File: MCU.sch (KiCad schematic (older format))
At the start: 25 parts, among them J1 Conn_ARM_SWD_NXP, J4 Conn_ARM_JTAG_SWD_20, U1 LPC54616J512, Y1 12MHz, Y2 32.768k

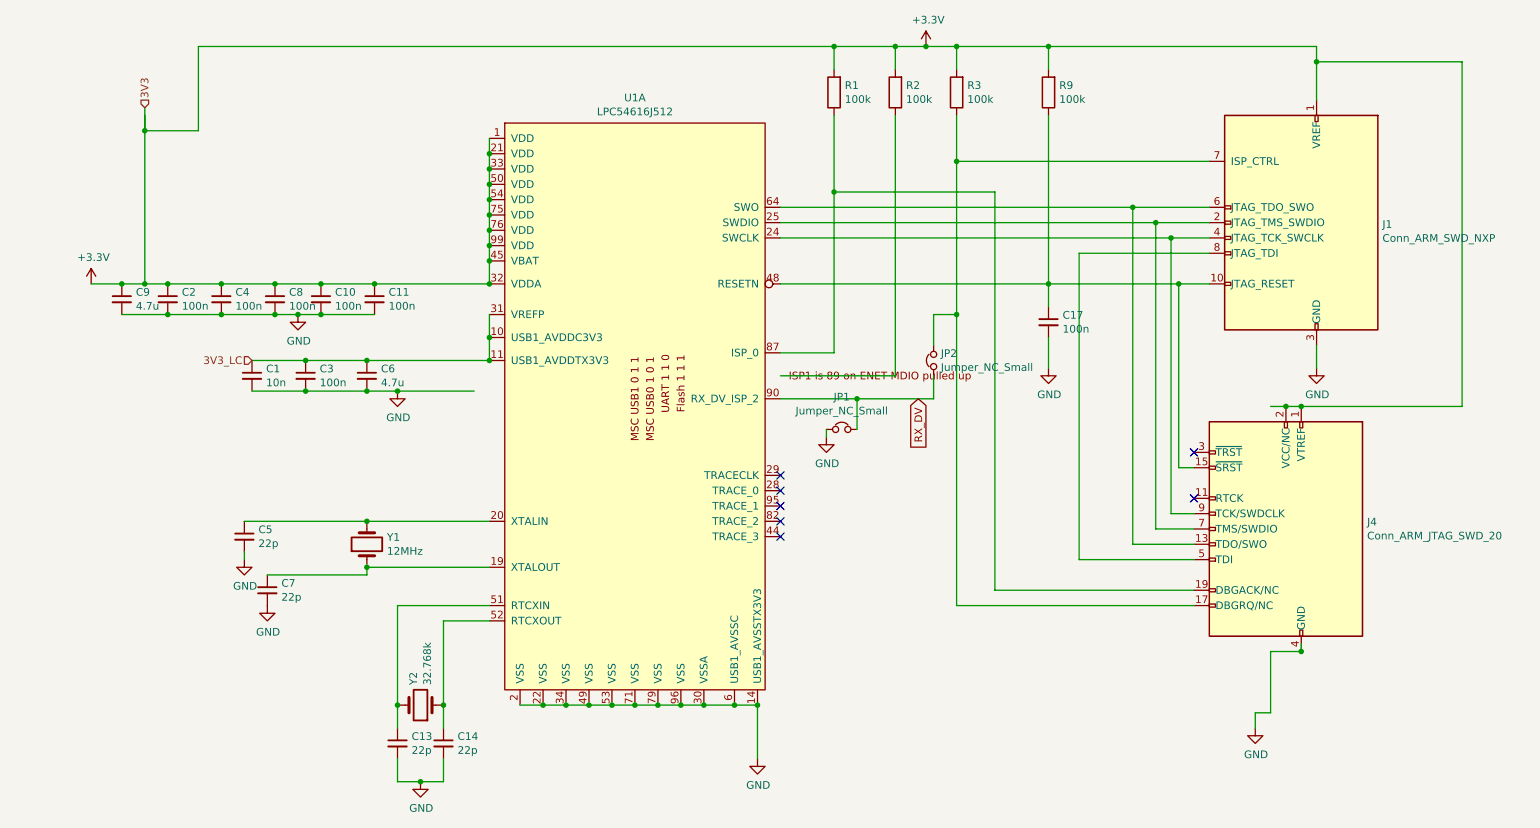
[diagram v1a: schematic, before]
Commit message: V3 bigger board, RMII instrumentation, inverter
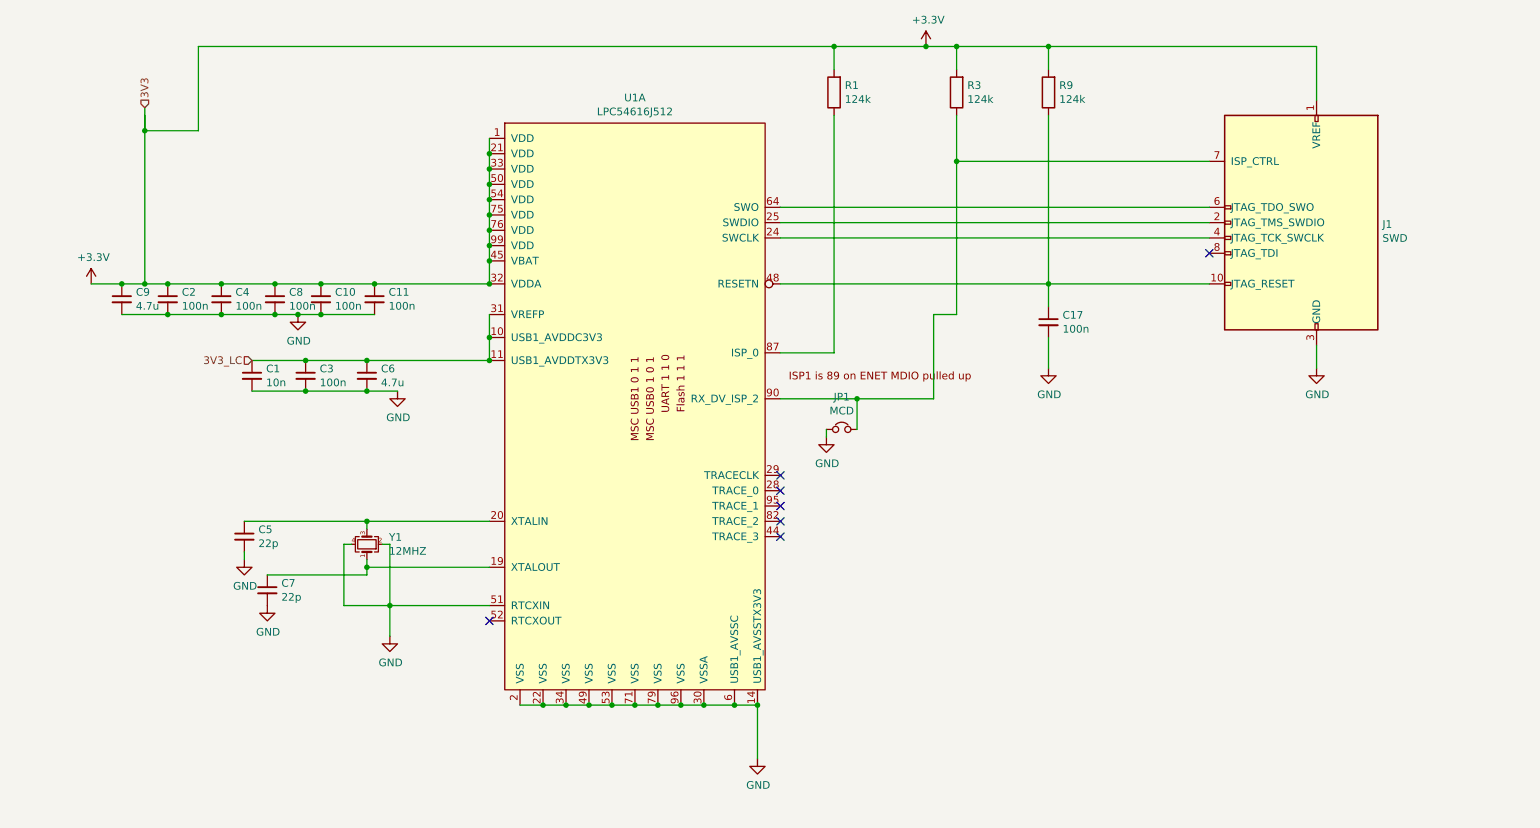
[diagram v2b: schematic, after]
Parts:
- removed C13, C14: 22p, Capacitor_SMD:C_0805_2012Metric_Pad1.15x1.40mm_HandSolder, symbol canbox-rescue:C_Small-Device
- removed J4: Conn_ARM_JTAG_SWD_20, Connector_IDC:IDC-Header_2x10_P2.54mm_Vertical, symbol canbox-rescue:Conn_ARM_JTAG_SWD_20-Connector
- removed JP2: Jumper_NC_Small, Connector_PinHeader_2.54mm:PinHeader_1x02_P2.54mm_Vertical, symbol canbox-rescue:Jumper_NC_Small-Device
- removed R2: 100k, Resistor_SMD:R_0805_2012Metric_Pad1.15x1.40mm_HandSolder, symbol canbox-rescue:R-Device
- removed Y1: 12MHz, Crystal:Crystal_HC49-4H_Vertical, symbol canbox-rescue:Crystal-Device
- removed Y2: 32.768k, Crystal:Crystal_DS26_D2.0mm_L6.0mm_Vertical, symbol canbox-rescue:Crystal-Device
- added Y1: 12MHZ, Crystal:Crystal_SMD_3225-4Pin_3.2x2.5mm_HandSoldering, symbol Device:Crystal_GND24_Small
- C1: JLC (none) -> C1710; OP C0805C103KCRACAUTO -> CL21B103KBANNNC
- C10, C11, C17, C2, C3, C4, C8: JLC (none) -> C49678; OP C0805C103K1RACTU -> CC0805KRX7R9BB104
- C5, C7: JLC (none) -> C1804; OP C0805C220J1GACTU -> CL21C220JBANNNC
- C6, C9: JLC (none) -> C1779; OP CL21A475KOFNNNG -> CL21A475KAQNNNE
- J1: value Conn_ARM_SWD_NXP -> SWD
- JP1: value Jumper_NC_Small -> MCD
- R1, R3, R9: value 100k -> 124k; JLC (none) -> C17440; OP CR0805-JW-104ELFCT-ND -> 0805W8F1243T5E
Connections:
- net labels removed: RX_DV
- wire segments 130 -> 91

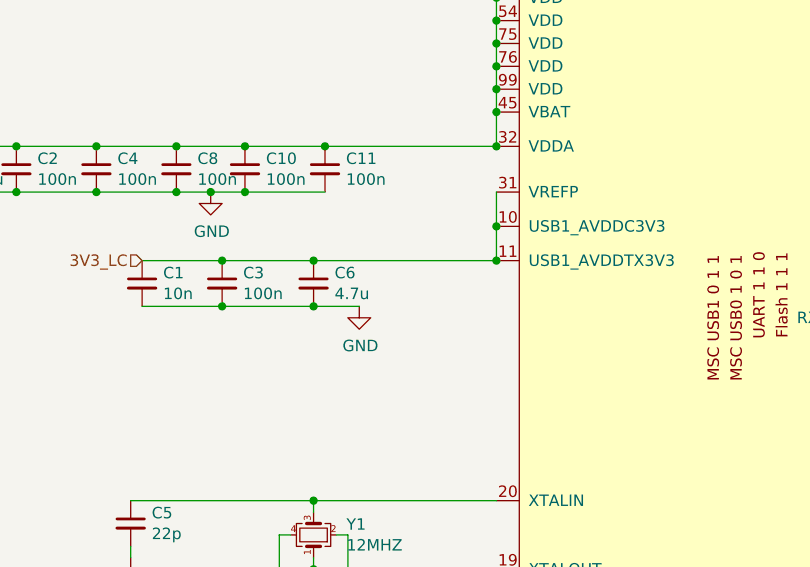
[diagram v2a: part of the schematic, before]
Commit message: Switch to 4 Layer PCB as the RMII loopback doesn't work
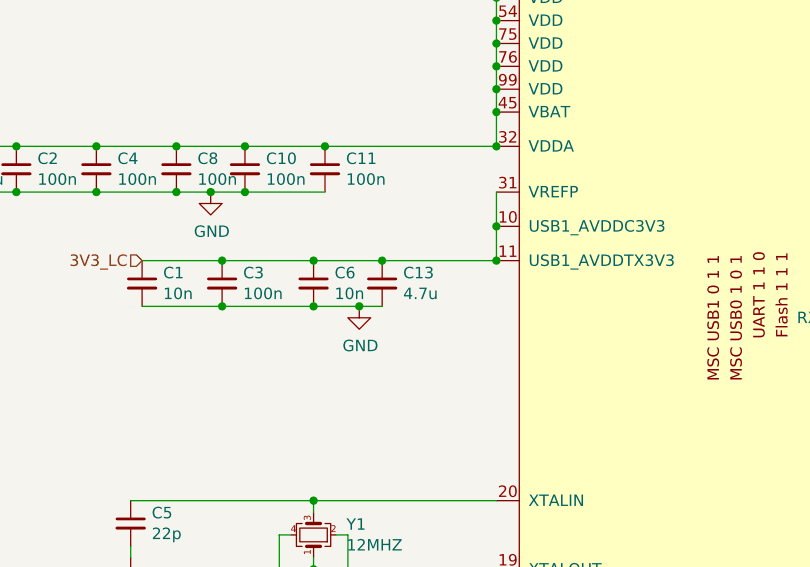
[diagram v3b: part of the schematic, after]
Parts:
- added C13: 4.7u, Capacitor_SMD:C_0805_2012Metric_Pad1.15x1.40mm_HandSolder, symbol canbox-rescue:C_Small-Device
- C6: value 4.7u -> 10n
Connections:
- net 3V3_LC: now also C13.1
- net GND: now also C13.2
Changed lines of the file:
@@
 P 3350 3100
 F 0 "C6" H 3442 3146 50  0000 L CNN
-F 1 "4.7u" H 3442 3055 50  0000 L CNN
+F 1 "10n" H 3442 3055 50  0000 L CNN
 F 2 "Capacitor_SMD:C_0805_2012Metric_Pad1.15x1.40mm_HandSolder" H 3350 3100 50  0001 C CNN
 F 3 "~" H 3350 3100 50  0001 C CNN
@@
 NoConn ~ 6050 4150
 Wire Wire Line
-	3350 3000 4150 3000
+	3350 3000 3650 3000
 $Comp
 L cypress:Conn_ARM_SWD_NXP J1
@@
 Wire Wire Line
 	3500 4600 4150 4600
+$Comp
+L canbox-rescue:C_Small-Device C13
+U 1 1 5E9F96CA
+P 3650 3100
+F 0 "C13" H 3742 3146 50  0000 L CNN
+F 1 "4.7u" H 3742 3055 50  0000 L CNN
+F 2 "Capacitor_SMD:C_0805_2012Metric_Pad1.15x1.40mm_HandSolder" H 3650 3100 50  0001 C CNN
+F 3 "~" H 3650 3100 50  0001 C CNN
+F 4 "CL21A475KAQNNNE" H 3650 3100 50  0001 C CNN "OP"
+F 5 "ali" H 300 0   50  0001 C CNN "notes"
+F 6 "C1779 " H 3650 3100 50  0001 C CNN "JLC"
+	1    3650 3100
+	1    0    0    -1
+$EndComp
+Connection ~ 3650 3000
+Wire Wire Line
+	3650 3000 4150 3000
+Wire Wire Line
+	3650 3200 3550 3200
+Connection ~ 3550 3200
 $EndSCHEMATC

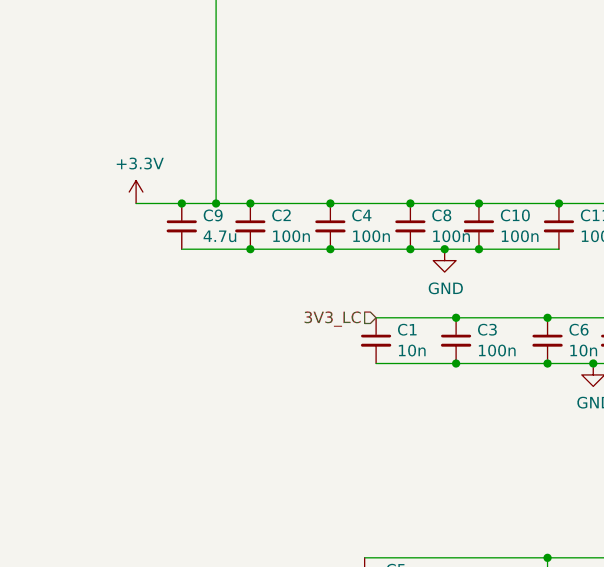
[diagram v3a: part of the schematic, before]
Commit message: V5 now impedance controlled
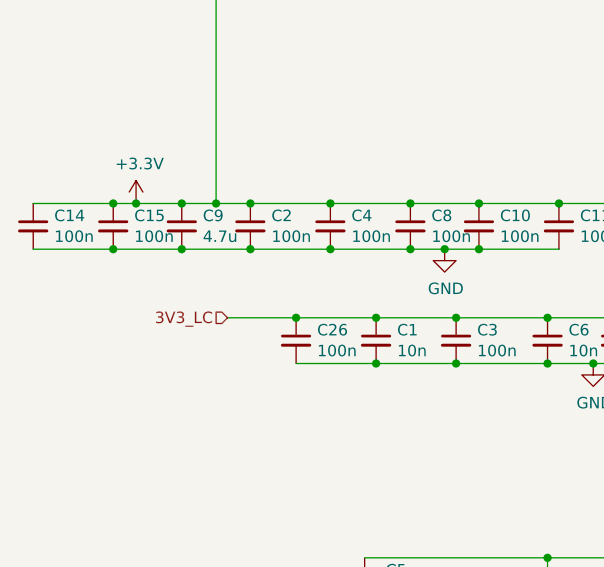
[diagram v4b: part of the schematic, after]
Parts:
- added C14, C15, C26: 100n, Capacitor_SMD:C_0805_2012Metric_Pad1.15x1.40mm_HandSolder, symbol canbox-rescue:C_Small-Device
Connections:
- net +3V3: now also C14.1, C15.1
- net 3V3_LC: now also C26.1
- net GND: now also C14.2, C15.2, C26.2
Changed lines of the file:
@@
 Wire Wire Line
 	6350 3500 6350 3450
-Text HLabel 2600 3000 0    50   Input ~ 0
+Text HLabel 1950 3000 0    50   Input ~ 0
 3V3_LC
 Wire Wire Line
@@
 Wire Wire Line
 	3350 3200 3550 3200
-Connection ~ 4150 2250
-Connection ~ 5400 5250
-Wire Wire Line
-	5250 5250 5400 5250
-Connection ~ 5250 5250
-Wire Wire Line
-	4150 2250 4150 2150
-Connection ~ 4150 2150
-Wire Wire Line
-	4150 2150 4150 2050
-Connection ~ 4150 2050
-Wire Wire Line
-	5100 5250 5250 5250
-Connection ~ 5100 5250
-Wire Wire Line
-	5750 5250 5900 5250
-Connection ~ 5750 5250
-Wire Wire Line
-	4150 2050 4150 1950
-Connection ~ 4150 1950
-Wire Wire Line
-	4950 5250 5100 5250
-Connection ~ 4950 5250
-Wire Wire Line
-	4150 1950 4150 1850
-Connection ~ 4150 1850
-Wire Wire Line
-	4800 5250 4950 5250
-Connection ~ 4800 5250
-Wire Wire Line
-	4150 2500 4150 2350
-Wire Wire Line
-	4150 2350 4150 2250
-Connection ~ 4150 2350
-Wire Wire Line
-	4650 5250 4800 5250
-Connection ~ 4650 5250
-Wire Wire Line
-	4150 1850 4150 1750
-Connection ~ 4150 1750
-Connection ~ 4150 2500
-Wire Wire Line
-	5550 5250 5750 5250
-Wire Wire Line
-	5400 5250 5550 5250
-Connection ~ 5550 5250
-Wire Wire Line
-	4500 5250 4650 5250
-Wire Wire Line
-	4350 5250 4500 5250
-Connection ~ 4500 5250
-Wire Wire Line
-	4150 1750 4150 1650
-Wire Wire Line
-	4150 1650 4150 1550
-Connection ~ 4150 1650
-Connection ~ 5900 5250
-Connection ~ 4150 3000
-Wire Wire Line
-	4150 2850 4150 2700
-Wire Wire Line
-	4150 3000 4150 2850
-Connection ~ 4150 2850
-$Comp
-L lpc_LPC54616J512:LPC54616J512 U1
-U 1 1 5BE7F06B
-P 4250 1450
-F 0 "U1" H 5100 1615 50  0000 C CNN
-F 1 "LPC54616J512" H 5100 1524 50  0000 C CNN
-F 2 "Package_QFP:LQFP-100_14x14mm_P0.5mm" H 4300 1300 50  0001 C CNN
-F 3 "" H 4300 1300 50  0001 C CNN
-F 4 "LPC54616J512BD100E" H 0   0   50  0001 C CNN "OP"
-F 5 "nm" H 0   0   50  0001 C CNN "Arrow"
-	1    4250 1450
-	1    0    0    -1
-$EndComp
 NoConn ~ 6050 3750
 NoConn ~ 6050 3850
@@
 	3650 3200 3550 3200
 Connection ~ 3550 3200
+$Comp
+L canbox-rescue:C_Small-Device C15
+U 1 1 5EACD5ED
+P 1450 2600
+F 0 "C15" H 1542 2646 50  0000 L CNN
+F 1 "100n" H 1542 2555 50  0000 L CNN
+F 2 "Capacitor_SMD:C_0805_2012Metric_Pad1.15x1.40mm_HandSolder" H 1450 2600 50  0001 C CNN
+F 3 "~" H 1450 2600 50  0001 C CNN
+F 4 "CC0805KRX7R9BB104" H 1450 2600 50  0001 C CNN "OP"
+F 5 "ali" H -1950 0   50  0001 C CNN "notes"
+F 6 " C49678 " H 1450 2600 50  0001 C CNN "JLC"
+	1    1450 2600
+	1    0    0    -1
+$EndComp
+$Comp
+L canbox-rescue:C_Small-Device C14
+U 1 1 5EAD2D64
+P 1100 2600
+F 0 "C14" H 1192 2646 50  0000 L CNN
+F 1 "100n" H 1192 2555 50  0000 L CNN
+F 2 "Capacitor_SMD:C_0805_2012Metric_Pad1.15x1.40mm_HandSolder" H 1100 2600 50  0001 C CNN
+F 3 "~" H 1100 2600 50  0001 C CNN
+F 4 "CC0805KRX7R9BB104" H 1100 2600 50  0001 C CNN "OP"
+F 5 "ali" H -2300 0   50  0001 C CNN "notes"
+F 6 " C49678 " H 1100 2600 50  0001 C CNN "JLC"
+	1    1100 2600
+	1    0    0    -1
+$EndComp
+$Comp
+L canbox-rescue:C_Small-Device C26
+U 1 1 5EAD5D3A
+P 2250 3100
+F 0 "C26" H 2342 3146 50  0000 L CNN
+F 1 "100n" H 2342 3055 50  0000 L CNN
+F 2 "Capacitor_SMD:C_0805_2012Metric_Pad1.15x1.40mm_HandSolder" H 2250 3100 50  0001 C CNN
+F 3 "~" H 2250 3100 50  0001 C CNN
+F 4 "CC0805KRX7R9BB104" H 2250 3100 50  0001 C CNN "OP"
+F 5 "ali" H -1150 500 50  0001 C CNN "notes"
+F 6 " C49678 " H 2250 3100 50  0001 C CNN "JLC"
+	1    2250 3100
+	1    0    0    -1
+$EndComp
+Wire Wire Line
+	1950 3000 2250 3000
+Connection ~ 2600 3000
+Connection ~ 2250 3000
+Wire Wire Line
+	2250 3000 2600 3000
+Wire Wire Line
+	2600 3200 2250 3200
+Connection ~ 2600 3200
+Wire Wire Line
+	1750 2700 1450 2700
+Connection ~ 1750 2700
+Connection ~ 1450 2700
+Wire Wire Line
+	1450 2700 1100 2700
+Wire Wire Line
+	1100 2500 1450 2500
+Connection ~ 1550 2500
+Connection ~ 1450 2500
+Wire Wire Line
+	1450 2500 1550 2500
+Connection ~ 4150 2850
+Wire Wire Line
+	4150 3000 4150 2850
+Wire Wire Line
+	4150 2850 4150 2700
+Connection ~ 4150 3000
+Connection ~ 5900 5250
+Connection ~ 4150 1650
+Wire Wire Line
+	4150 1650 4150 1550
+Connection ~ 4500 5250
+Wire Wire Line
+	4350 5250 4500 5250
+Connection ~ 5550 5250
+Wire Wire Line
+	5400 5250 5550 5250
+Connection ~ 4150 2500
+Connection ~ 4150 1750
+Wire Wire Line
+	4150 1750 4150 1650
+Wire Wire Line
+	4150 1850 4150 1750
+Connection ~ 4650 5250
+Wire Wire Line
+	4500 5250 4650 5250
+Wire Wire Line
+	4650 5250 4800 5250
+Connection ~ 4150 2350
+Wire Wire Line
+	4150 2350 4150 2250
+Wire Wire Line
+	4150 2500 4150 2350
+Connection ~ 4800 5250
+Connection ~ 4150 1850
+Connection ~ 4950 5250
+Wire Wire Line
+	4800 5250 4950 5250
+Wire Wire Line
+	4950 5250 5100 5250
+Connection ~ 4150 1950
+Wire Wire Line
+	4150 1950 4150 1850
+Wire Wire Line
+	4150 2050 4150 1950
+Connection ~ 5750 5250
+Wire Wire Line
+	5550 5250 5750 5250
+Wire Wire Line
+	5750 5250 5900 5250
+Connection ~ 5100 5250
+Connection ~ 4150 2050
+Connection ~ 4150 2150
+Wire Wire Line
+	4150 2150 4150 2050
+Wire Wire Line
+	4150 2250 4150 2150
+Connection ~ 5250 5250
+Wire Wire Line
+	5100 5250 5250 5250
+Wire Wire Line
+	5250 5250 5400 5250
+Connection ~ 5400 5250
+Connection ~ 4150 2250
+$Comp
+L lpc_LPC54616J512:LPC54616J512 U1
+U 1 1 5BE7F06B
+P 4250 1450
+F 0 "U1" H 5100 1615 50  0000 C CNN
+F 1 "LPC54616J512" H 5100 1524 50  0000 C CNN
+F 2 "Package_QFP:LQFP-100_14x14mm_P0.5mm" H 4300 1300 50  0001 C CNN
+F 3 "" H 4300 1300 50  0001 C CNN
+F 4 "LPC54616J512BD100E" H 0   0   50  0001 C CNN "OP"
+F 5 "nm" H 0   0   50  0001 C CNN "Arrow"
+	1    4250 1450
+	1    0    0    -1
+$EndComp
 $EndSCHEMATC
